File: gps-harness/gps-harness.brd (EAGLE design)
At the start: 25.1 x 34.3 mm, 7 parts

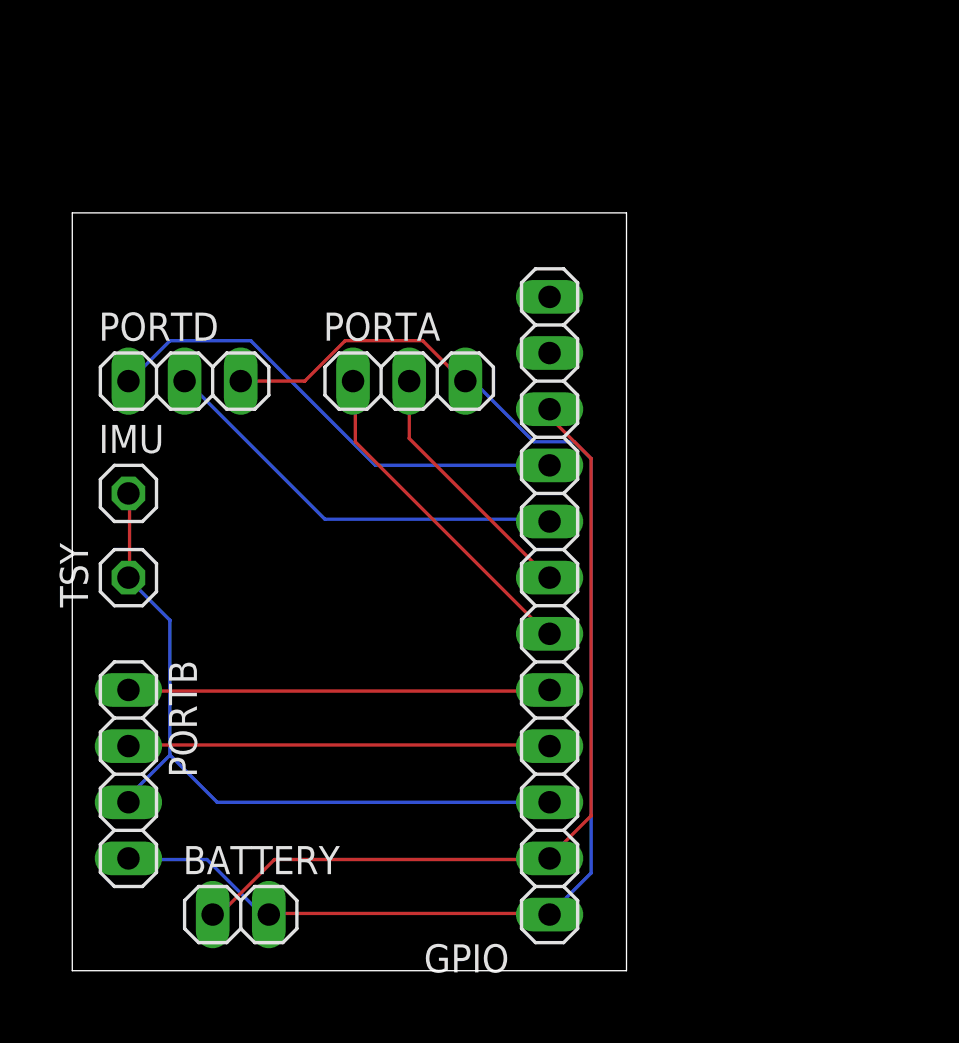
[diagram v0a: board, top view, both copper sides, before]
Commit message: Fixed the width of the wires for battery and trying to do the mounting holes
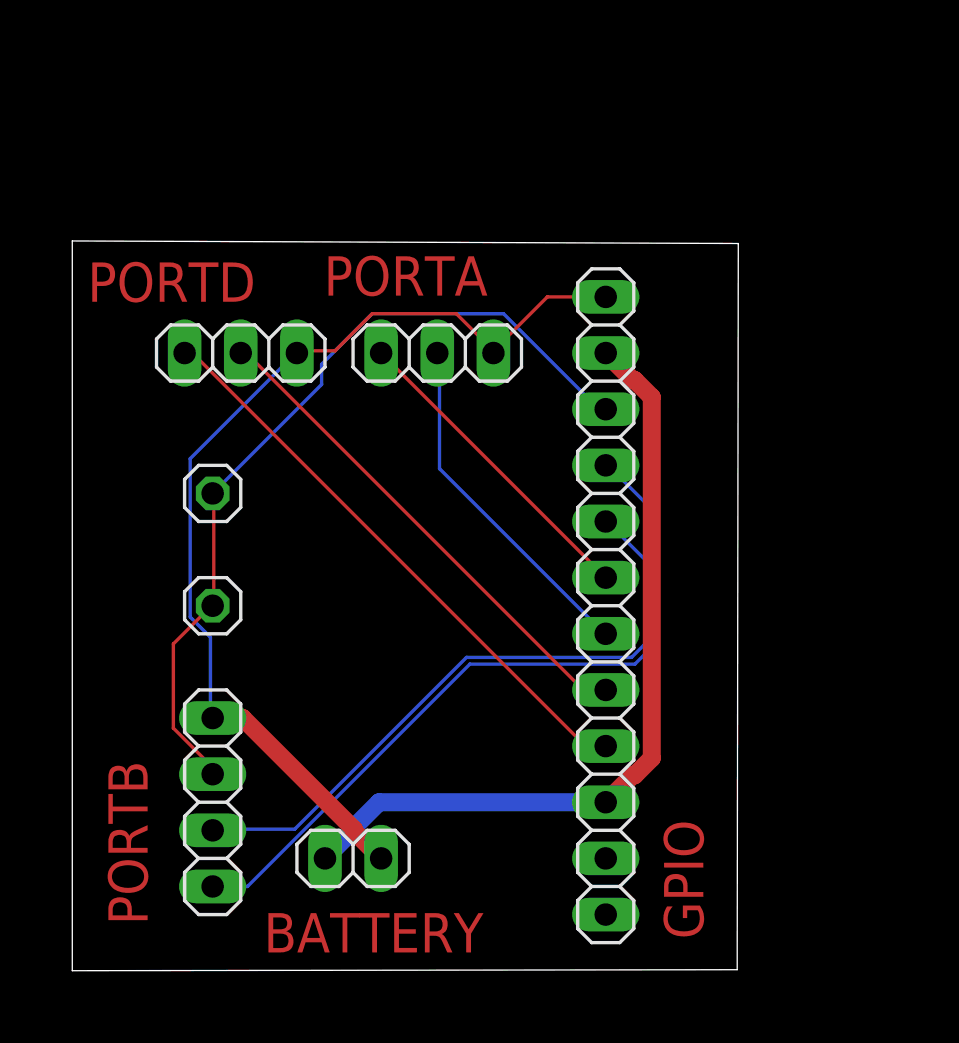
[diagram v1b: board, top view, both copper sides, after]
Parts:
- moved BATTERY 5.68 mm to (12.7, 5.08)
- moved PORTB 4.02 mm to (6.35, 7.62), turned to 90 degrees
- moved TSY 4.02 mm to (6.35, 16.5), turned to 0 degrees
- moved IMU 3.81 mm to (6.35, 21.6)
- moved PORTD 2.84 mm to (7.62, 27.9)
- moved GPIO 2.54 mm to (24.1, 16.5), turned to 270 degrees
- moved PORTA 1.80 mm to (16.5, 27.9)
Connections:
- net N$1 renamed IMU
- net RX renamed RXA
- net TX renamed TXA
- new net N$23: GPIO.11
- new net N$24: GPIO.12
- net GND: now also BATTERY.2, GPIO.1, PORTA.3, PORTB.4, PORTD.3; no longer BATTERY.1, GPIO.10, GPIO.2
- net RXB: now also GPIO.5, PORTB.2; no longer GPIO.8, PORTD.2
- net RXD: now also GPIO.8, PORTD.2; no longer GPIO.4, PORTB.2
- net TXB: now also GPIO.4, PORTB.1; no longer GPIO.9, PORTD.1
- net TXD: now also GPIO.9, PORTD.1; no longer GPIO.5, PORTB.1
- net VCC: now also BATTERY.1, GPIO.10, GPIO.2; no longer BATTERY.2, GPIO.1, PORTA.3, PORTB.4, PORTD.3
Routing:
- net VCC: track 60.3 -> 36.0 mm
- net TXB: track 22.1 -> 33.5 mm
- net RXB: track 19.1 -> 29.3 mm
- net GND: track 38.1 -> 45.8 mm
- net TXD: track 19.1 -> 26.4 mm
- net RXA: track 11.5 -> 15.9 mm
- net IMU: track 33.6 -> 37.7 mm
- net RXD: track 19.1 -> 22.9 mm
- net TXA: track 15.2 -> 14.4 mm
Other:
- board size 25.1 x 34.3 mm -> 30.1 x 33 mm
- board text added: "BATTERY"
- board text added: "GPIO"
- board text added: "PORTA"
- board text added: "PORTB"
- board text added: "PORTD"

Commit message: Trying to choose the connector
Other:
- board size 30.1 x 33 mm -> 30.1 x 33.1 mm
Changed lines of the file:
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@@
 <layer number="28" name="bValues" color="7" fill="1" visible="yes" active="yes"/>
 <layer number="29" name="tStop" color="7" fill="3" visible="no" active="yes"/>
-<layer number="30" name="bStop" color="7" fill="6" visible="no" active="yes"/>
+<layer number="30" name="bStop" color="7" fill="6" visible="yes" active="yes"/>
 <layer number="31" name="tCream" color="7" fill="4" visible="no" active="yes"/>
 <layer number="32" name="bCream" color="7" fill="5" visible="no" active="yes"/>
@@
 <plain>
 <wire x1="0" y1="0" x2="30.0763375" y2="0.04571875" width="0" layer="20"/>
-<wire x1="30.0763375" y1="0.04571875" x2="30.127103125" y2="32.895340625" width="0" layer="20"/>
-<wire x1="30.127103125" y1="32.895340625" x2="0" y2="33.01" width="0" layer="20"/>
+<wire x1="30.0763375" y1="0.04571875" x2="30.127103125" y2="33.078221875" width="0" layer="20"/>
+<wire x1="30.127103125" y1="33.078221875" x2="0" y2="33.01" width="0" layer="20"/>
 <wire x1="0" y1="33.01" x2="0" y2="0" width="0" layer="20"/>
-<text x="0.688340625" y="30.259021875" size="1.778" layer="1">PORTD</text>
-<text x="11.37411875" y="30.53841875" size="1.778" layer="1">PORTA</text>
-<text x="3.408678125" y="2.072640625" size="1.778" layer="1" rot="R90">PORTB</text>
-<text x="8.65631875" y="0.828040625" size="1.778" layer="1">BATTERY</text>
-<text x="28.5470625" y="1.42748125" size="1.778" layer="1" rot="R90">GPIO</text>
+<text x="3.924303125" y="25.425403125" size="0.4064" layer="1">PORTD</text>
+<text x="13.149578125" y="25.430478125" size="0.4064" layer="1">PORTA</text>
+<text x="7.00785625" y="2.1183625" size="0.4064" layer="1" rot="R180">PORTB</text>
+<text x="11.84655625" y="2.37998125" size="0.4064" layer="1">BATTERY</text>
+<text x="23.489921875" y="32.209740625" size="0.4064" layer="1">GPIO</text>
 </plain>
 <attributes>
@@
 <contactref element="BATTERY" pad="2"/>
 <wire x1="11.8872" y1="28.0416" x2="10.2108" y2="28.0416" width="0.1524" layer="1"/>
-<wire x1="13.5636" y1="29.718" x2="11.8872" y2="28.0416" width="0.1524" layer="1"/>
+<wire x1="11.8872" y1="28.0416" x2="13.5636" y2="29.718" width="0.1524" layer="1"/>
 <wire x1="17.3736" y1="29.718" x2="13.5636" y2="29.718" width="0.1524" layer="1"/>
-<wire x1="19.05" y1="28.0416" x2="17.3736" y2="29.718" width="0.1524" layer="1"/>
+<wire x1="17.3736" y1="29.718" x2="19.05" y2="28.0416" width="0.1524" layer="1"/>
 <wire x1="10.2108" y1="28.0416" x2="10.16" y2="27.94" width="0.1524" layer="1"/>
 <wire x1="21.4884" y1="30.48" x2="24.13" y2="30.48" width="0.1524" layer="1"/>
@@
 <wire x1="6.2484" y1="11.43" x2="6.35" y2="11.43" width="0.1524" layer="16"/>
 <wire x1="10.0584" y1="27.8892" x2="10.16" y2="27.94" width="0.1524" layer="16"/>
-<wire x1="13.97" y1="5.08" x2="12.7508" y2="6.2992" width="0.8128" layer="1"/>
-<wire x1="12.7508" y1="6.2992" x2="12.7508" y2="6.38909375" width="0.8128" layer="1"/>
-<wire x1="12.7508" y1="6.38909375" x2="7.70989375" y2="11.43" width="0.8128" layer="1"/>
-<wire x1="7.70989375" y1="11.43" x2="6.35" y2="11.43" width="0.8128" layer="1"/>
+<wire x1="6.35" y1="11.43" x2="7.62" y2="11.43" width="0.6096" layer="1"/>
+<wire x1="7.62" y1="11.43" x2="13.97" y2="5.08" width="0.6096" layer="1"/>
 </signal>
 <signal name="RXA">
@@
 <contactref element="GPIO" pad="2"/>
 <contactref element="GPIO" pad="10"/>
-<wire x1="24.03601875" y1="7.62" x2="24.13" y2="7.62" width="0.3048" layer="16"/>
-<wire x1="25.43909375" y1="26.7208" x2="26.2128" y2="25.94709375" width="0.8128" layer="1"/>
-<wire x1="26.2128" y1="9.61290625" x2="25.43909375" y2="8.8392" width="0.8128" layer="1"/>
-<wire x1="24.13" y1="27.94" x2="25.3492" y2="26.7208" width="0.8128" layer="1"/>
-<wire x1="25.3492" y1="26.7208" x2="25.43909375" y2="26.7208" width="0.8128" layer="1"/>
-<wire x1="25.43909375" y1="8.8392" x2="25.3492" y2="8.8392" width="0.8128" layer="1"/>
-<wire x1="25.3492" y1="8.8392" x2="24.13" y2="7.62" width="0.8128" layer="1"/>
-<wire x1="26.2128" y1="25.94709375" x2="26.2128" y2="9.61290625" width="0.8128" layer="1"/>
-<wire x1="11.43" y1="5.08" x2="12.6492" y2="6.2992" width="0.8128" layer="16"/>
-<wire x1="12.6492" y1="6.2992" x2="12.6492" y2="6.38909375" width="0.8128" layer="16"/>
-<wire x1="12.6492" y1="6.38909375" x2="13.88010625" y2="7.62" width="0.8128" layer="16"/>
-<wire x1="13.88010625" y1="7.62" x2="24.03601875" y2="7.62" width="0.8128" layer="16"/>
+<wire x1="24.03601875" y1="7.62" x2="24.107140625" y2="7.62" width="0.3048" layer="16"/>
+<wire x1="24.107140625" y1="7.62" x2="24.13" y2="7.62" width="0.3048" layer="16"/>
+<wire x1="26.1112" y1="25.9050125" x2="26.0223" y2="25.9939125" width="0.6096" layer="1"/>
+<wire x1="26.0223" y1="25.9939125" x2="26.0223" y2="26.222959375" width="0.6096" layer="1"/>
+<wire x1="24.13" y1="7.62" x2="26.1112" y2="9.6012" width="0.6096" layer="1"/>
+<wire x1="26.1112" y1="9.6012" x2="26.1112" y2="25.9050125" width="0.6096" layer="1"/>
+<wire x1="26.0223" y1="26.222959375" x2="24.305259375" y2="27.94" width="0.6096" layer="1"/>
+<wire x1="24.305259375" y1="27.94" x2="24.13" y2="27.94" width="0.6096" layer="1"/>
+<wire x1="11.43" y1="5.08" x2="13.97" y2="7.62" width="0.6096" layer="16"/>
+<wire x1="13.97" y1="7.62" x2="24.107140625" y2="7.62" width="0.6096" layer="16"/>
 </signal>
 <signal name="TXD">

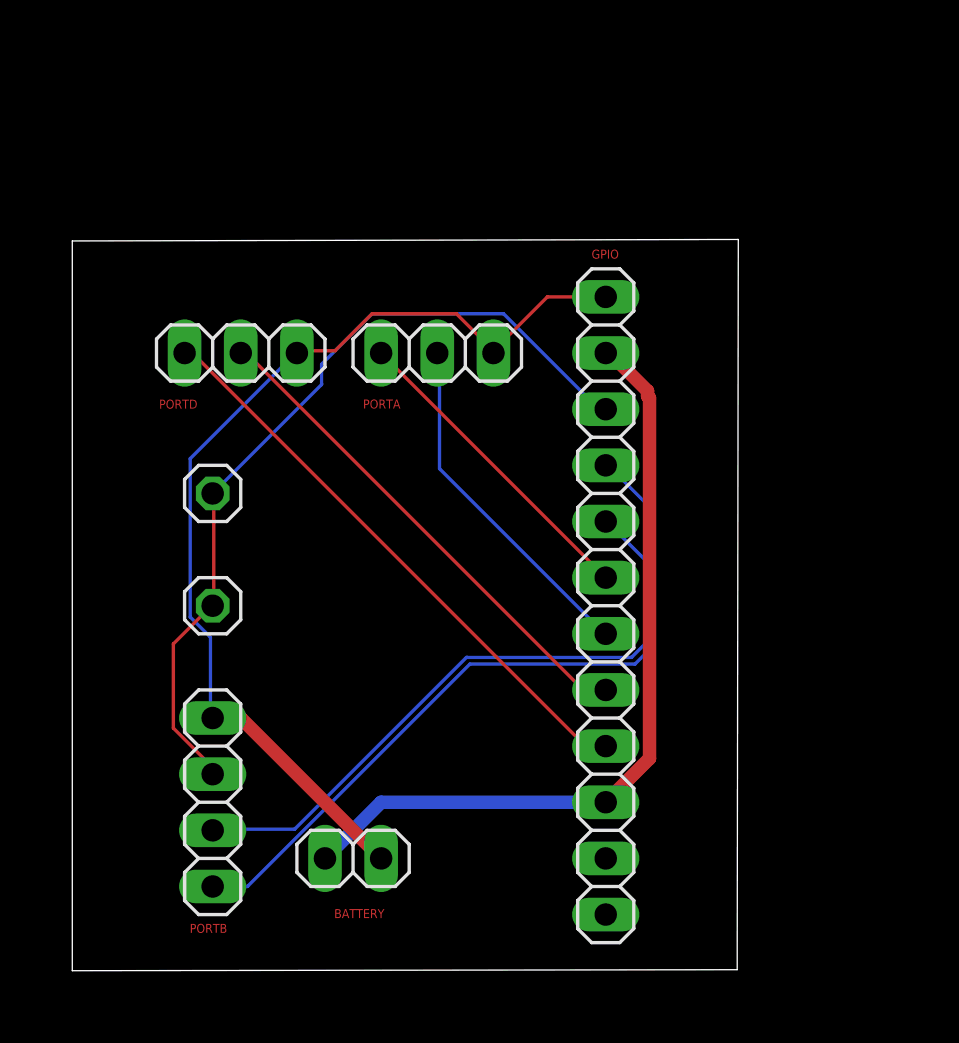
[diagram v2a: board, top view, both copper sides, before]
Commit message: Mounting holes
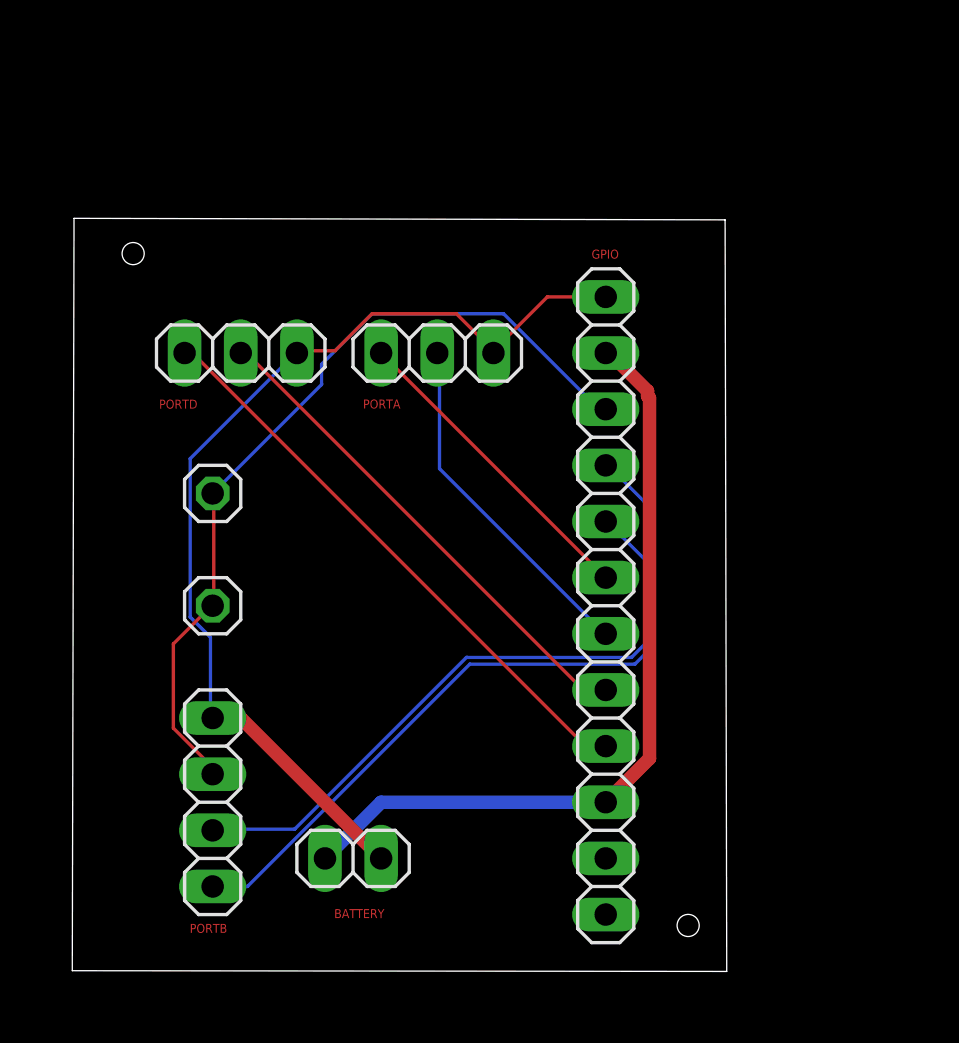
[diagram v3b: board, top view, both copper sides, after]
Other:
- board size 30.1 x 33.1 mm -> 29.6 x 34.1 mm
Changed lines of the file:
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@@
 <layer number="43" name="vRestrict" color="2" fill="10" visible="yes" active="yes"/>
 <layer number="44" name="Drills" color="7" fill="1" visible="no" active="yes"/>
-<layer number="45" name="Holes" color="7" fill="1" visible="no" active="yes"/>
+<layer number="45" name="Holes" color="7" fill="1" visible="yes" active="yes"/>
 <layer number="46" name="Milling" color="3" fill="1" visible="no" active="yes"/>
 <layer number="47" name="Measures" color="7" fill="1" visible="no" active="yes"/>
@@
 <board>
 <plain>
-<wire x1="0" y1="0" x2="30.0763375" y2="0.04571875" width="0" layer="20"/>
-<wire x1="30.0763375" y1="0.04571875" x2="30.127103125" y2="33.078221875" width="0" layer="20"/>
-<wire x1="30.127103125" y1="33.078221875" x2="0" y2="33.01" width="0" layer="20"/>
-<wire x1="0" y1="33.01" x2="0" y2="0" width="0" layer="20"/>
+<wire x1="0" y1="0" x2="29.603896875" y2="-0.033021875" width="0" layer="20"/>
+<wire x1="29.603896875" y1="-0.033021875" x2="29.53020625" y2="33.964684375" width="0" layer="20"/>
+<wire x1="29.53020625" y1="33.964684375" x2="0.078740625" y2="34.033621875" width="0" layer="20"/>
+<wire x1="0.078740625" y1="34.033621875" x2="0" y2="0" width="0" layer="20"/>
 <text x="3.924303125" y="25.425403125" size="0.4064" layer="1">PORTD</text>
 <text x="13.149578125" y="25.430478125" size="0.4064" layer="1">PORTA</text>
@@
 <text x="11.84655625" y="2.37998125" size="0.4064" layer="1">BATTERY</text>
 <text x="23.489921875" y="32.209740625" size="0.4064" layer="1">GPIO</text>
+<hole x="2.753359375" y="32.438340625" drill="1" locked="yes"/>
+<hole x="27.858721875" y="2.047240625" drill="1" locked="yes"/>
 </plain>
 <attributes>
@@
 packages will not be understood (or retained) with this version.
 </note>
+<note version="8.5" severity="warning">
+Since Version 8.5, EAGLE supports locking for holes, vias, wires and polygons.
+The locking property on all objects of these types will not be understood in this version.
+</note>
 </compatibility>

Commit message: Add CSV File
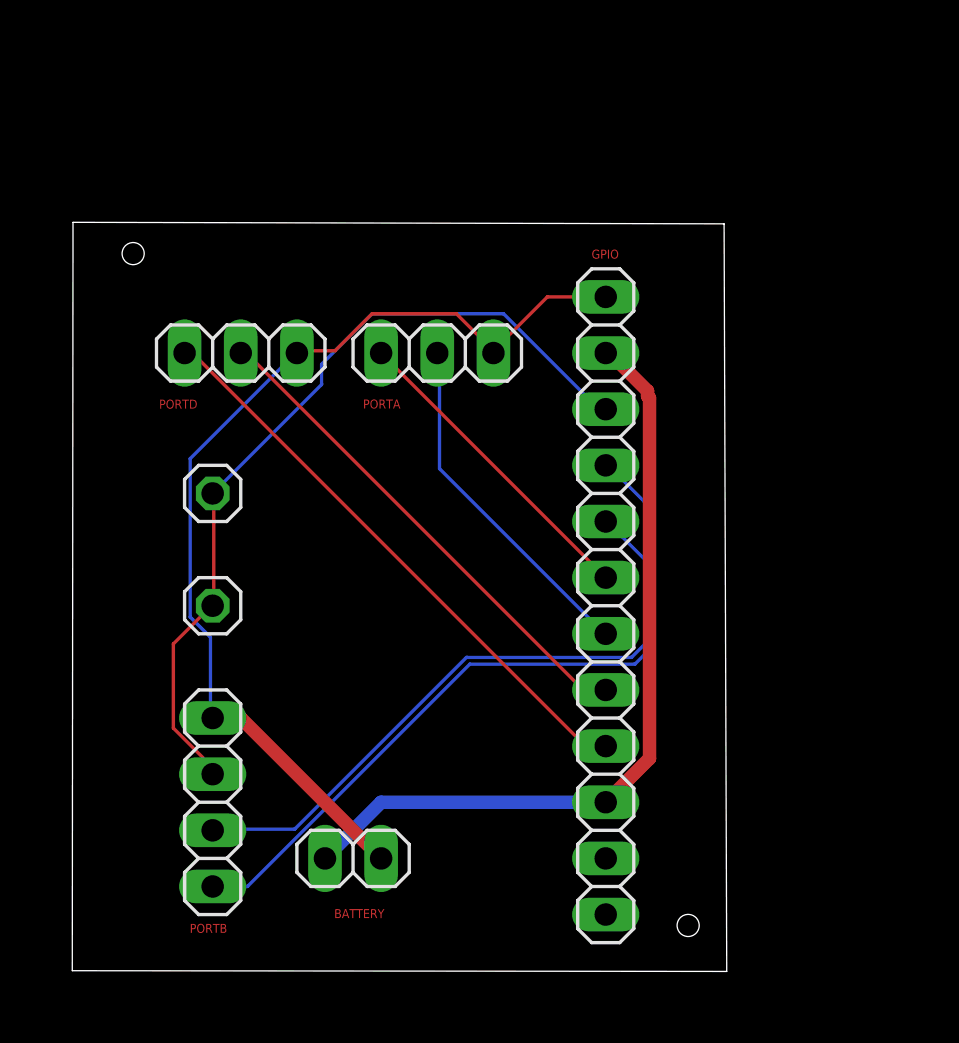
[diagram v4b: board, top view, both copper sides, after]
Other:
- board size 29.6 x 34.1 mm -> 29.6 x 33.9 mm
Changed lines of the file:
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@@
 <plain>
 <wire x1="0" y1="0" x2="29.603896875" y2="-0.033021875" width="0" layer="20"/>
-<wire x1="29.603896875" y1="-0.033021875" x2="29.53020625" y2="33.964684375" width="0" layer="20"/>
-<wire x1="29.53020625" y1="33.964684375" x2="0.078740625" y2="34.033621875" width="0" layer="20"/>
-<wire x1="0.078740625" y1="34.033621875" x2="0" y2="0" width="0" layer="20"/>
+<wire x1="29.603896875" y1="-0.033021875" x2="29.4844875" y2="33.784346875" width="0" layer="20"/>
+<wire x1="29.4844875" y1="33.784346875" x2="0.033021875" y2="33.853284375" width="0" layer="20"/>
+<wire x1="0.033021875" y1="33.853284375" x2="0" y2="0" width="0" layer="20"/>
 <text x="3.924303125" y="25.425403125" size="0.4064" layer="1">PORTD</text>
 <text x="13.149578125" y="25.430478125" size="0.4064" layer="1">PORTA</text>
